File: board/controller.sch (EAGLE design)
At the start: 70 parts, among them J1 X, J10 FEED_HOLD, J11 PROBE, J12 ERROR, J13 HOLDING, J14 GND, J15 MOTOR_CURRENT, J16 SD_READER, J17 WHEEL, J18 FEED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

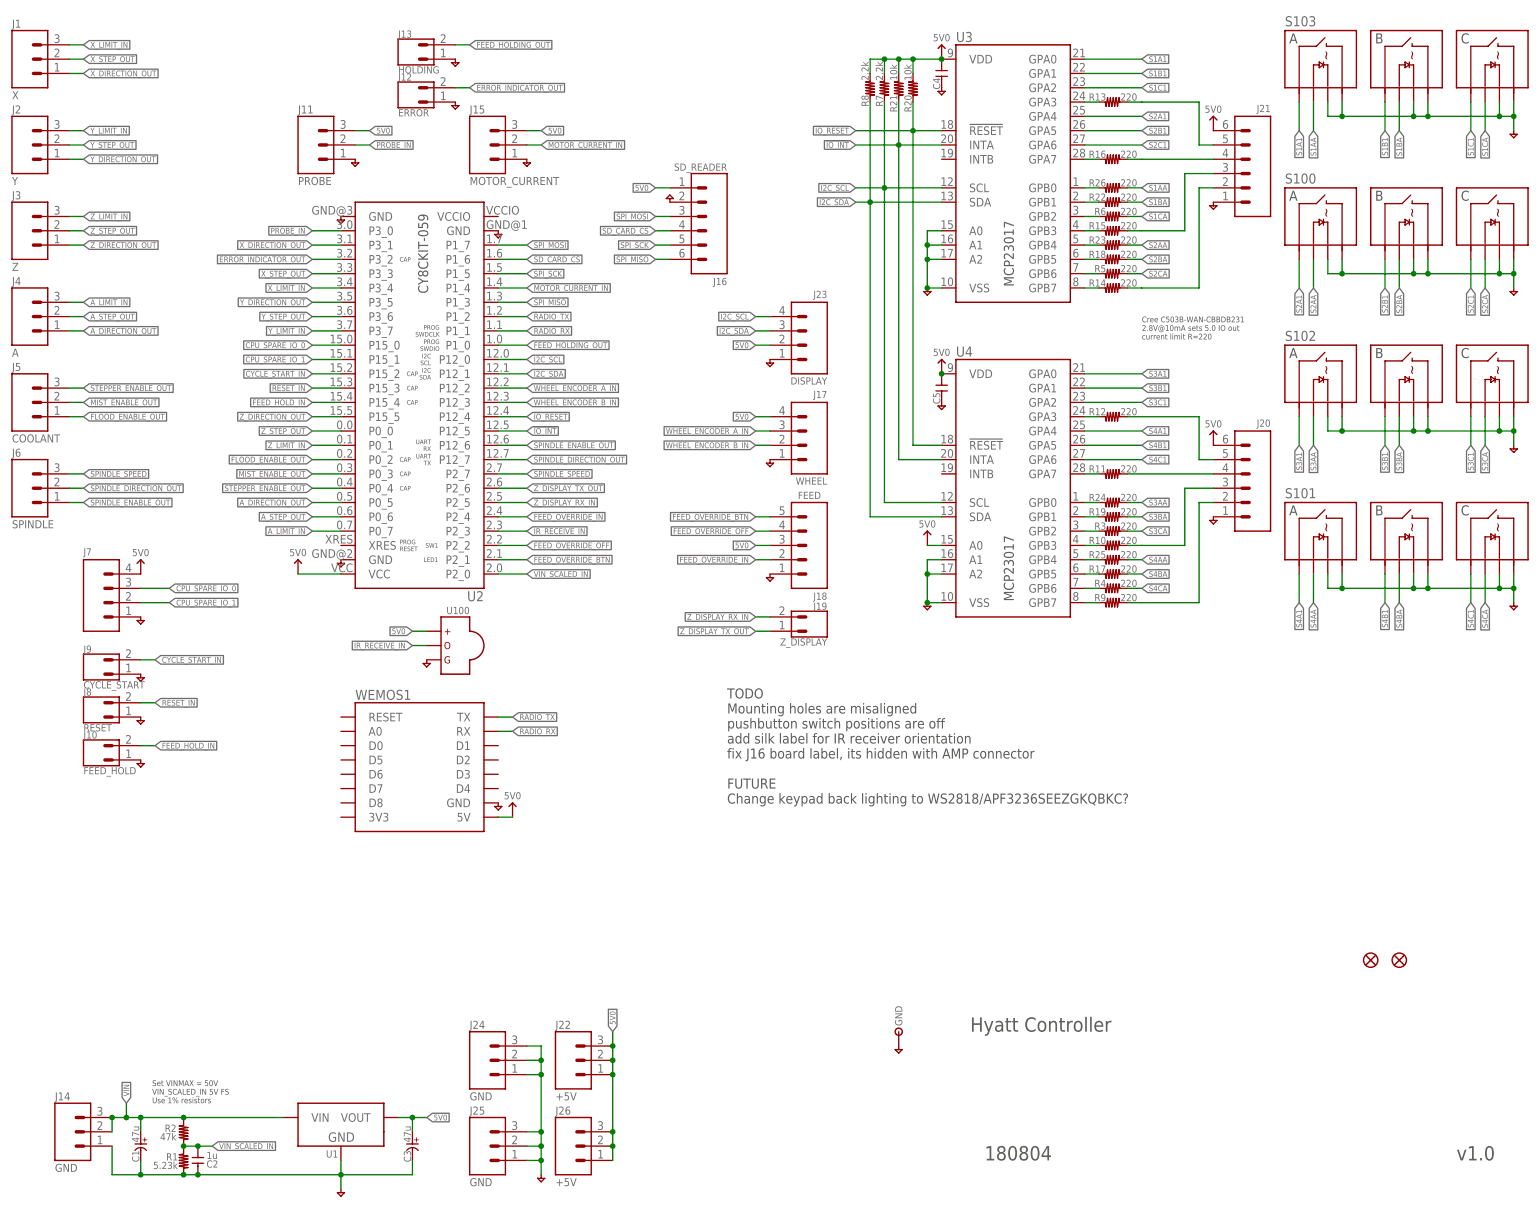
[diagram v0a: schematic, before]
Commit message: a little cleaning in main.c started v1.1 of schematic, v1.0 boards need blue-wired
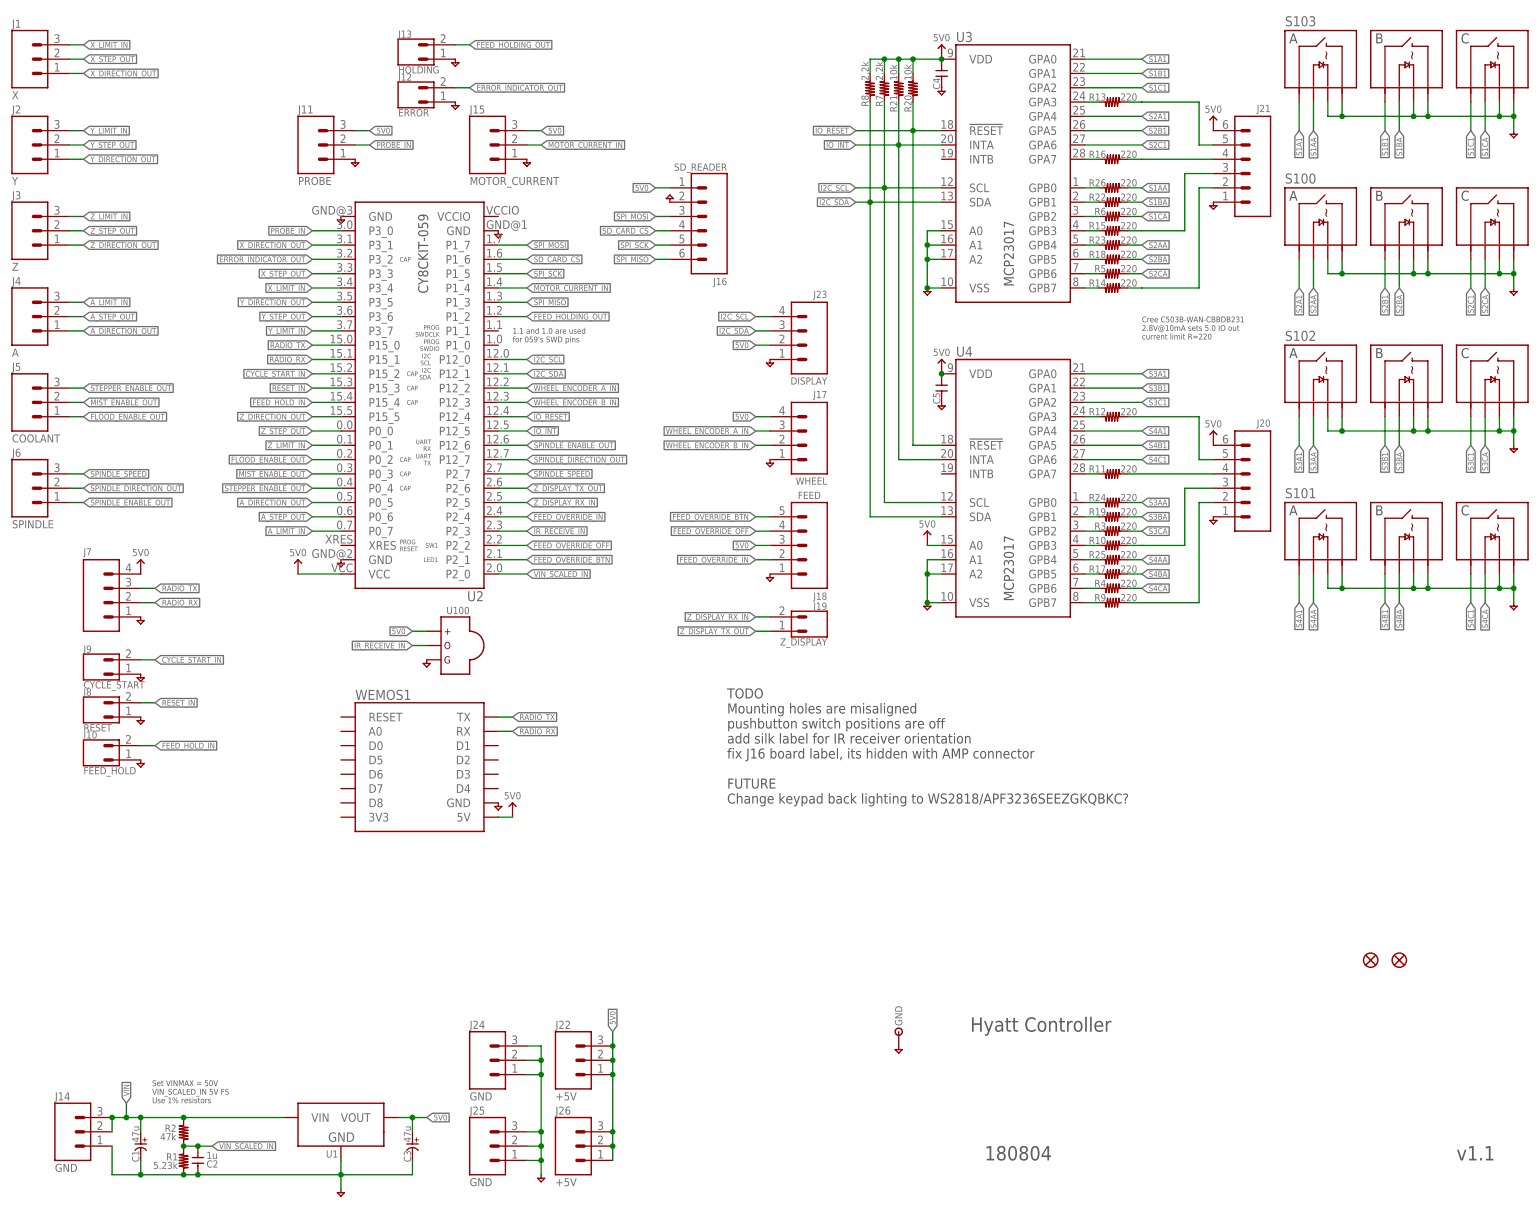
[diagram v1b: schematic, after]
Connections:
- removed net CPU_SPARE_IO_0: J7.3, U2.P15_0
- removed net CPU_SPARE_IO_1: J7.2, U2.P15_1
- net FEED_HOLDING_OUT: now also U2.P1_2; no longer U2.P1_0
- net RADIO_RX: now also J7.2, U2.P15_1; no longer U2.P1_1
- net RADIO_TX: now also J7.3, U2.P15_0; no longer U2.P1_2
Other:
- note added: "1.1 and 1.0 are used for 059's SWD pins"
- note added: "v1.1"
- note removed: "v1.0"
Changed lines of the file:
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@@
 <setting verticaltext="up"/>
 </settings>
-<grid distance="0.1" unitdist="inch" unit="inch" style="lines" multiple="1" display="yes" altdistance="0.01" altunitdist="inch" altunit="inch"/>
+<grid distance="0.1" unitdist="inch" unit="inch" style="lines" multiple="1" display="no" altdistance="0.01" altunitdist="inch" altunit="inch"/>
 <layers>
 <layer number="1" name="Top" color="4" fill="1" visible="no" active="no"/>
@@
 <text x="175.26" y="33.02" size="2.54" layer="97" align="top-left">Hyatt Controller</text>
 <text x="177.8" y="10.16" size="2.54" layer="97" align="top-left">180804</text>
-<text x="261.62" y="10.16" size="2.54" layer="97" align="top-left">v1.0</text>
+<text x="261.62" y="10.16" size="2.54" layer="97" align="top-left">v1.1</text>
 <text x="132.08" y="91.44" size="1.778" layer="97" align="top-left">TODO
 Mounting holes are misaligned
@@
 VIN_SCALED_IN 5V FS
 Use 1% resistors</text>
+<text x="93.98" y="155.448" size="1.016" layer="97" align="top-left">1.1 and 1.0 are used
+for 059's SWD pins</text>
 </plain>
 <instances>
@@
 </segment>
 <segment>
-<pinref part="U2" gate="G$1" pin="P1_0"/>
-<wire x1="91.44" y1="152.4" x2="96.52" y2="152.4" width="0.1524" layer="91"/>
-<label x="96.52" y="152.4" size="1.016" layer="95" xref="yes"/>
+<label x="96.52" y="157.48" size="1.016" layer="95" xref="yes"/>
+<pinref part="U2" gate="G$1" pin="P1_2"/>
+<wire x1="91.44" y1="157.48" x2="96.52" y2="157.48" width="0.1524" layer="91"/>
 </segment>
 </net>
@@
 </segment>
 <segment>
-<pinref part="U2" gate="G$1" pin="P1_2"/>
-<wire x1="91.44" y1="157.48" x2="96.52" y2="157.48" width="0.1524" layer="91"/>
-<label x="96.52" y="157.48" size="1.016" layer="95" xref="yes"/>
+<pinref part="U2" gate="G$1" pin="P15_0"/>
+<wire x1="63.5" y1="152.4" x2="58.42" y2="152.4" width="0.1524" layer="91"/>
+<label x="58.42" y="152.4" size="1.016" layer="95" rot="R180" xref="yes"/>
+</segment>
+<segment>
+<pinref part="J7" gate="G$1" pin="3"/>
+<wire x1="27.94" y1="109.22" x2="30.48" y2="109.22" width="0.1524" layer="91"/>
+<label x="30.48" y="109.22" size="1.016" layer="95" xref="yes"/>
 </segment>
 </net>
@@
 </segment>
 <segment>
-<pinref part="U2" gate="G$1" pin="P1_1"/>
-<wire x1="91.44" y1="154.94" x2="96.52" y2="154.94" width="0.1524" layer="91"/>
-<label x="96.52" y="154.94" size="1.016" layer="95" xref="yes"/>
+<pinref part="U2" gate="G$1" pin="P15_1"/>
+<wire x1="63.5" y1="149.86" x2="58.42" y2="149.86" width="0.1524" layer="91"/>
+<label x="58.42" y="149.86" size="1.016" layer="95" rot="R180" xref="yes"/>
+</segment>
+<segment>
+<pinref part="J7" gate="G$1" pin="2"/>
+<wire x1="27.94" y1="106.68" x2="30.48" y2="106.68" width="0.1524" layer="91"/>
+<label x="30.48" y="106.68" size="1.016" layer="95" xref="yes"/>
 </segment>
 </net>
@@
 </segment>
 </net>
-<net name="CPU_SPARE_IO_0" class="0">
-<segment>
-<pinref part="J7" gate="G$1" pin="3"/>
-<wire x1="27.94" y1="109.22" x2="33.02" y2="109.22" width="0.1524" layer="91"/>
-<label x="33.02" y="109.22" size="1.016" layer="95" xref="yes"/>
-</segment>
-<segment>
-<pinref part="U2" gate="G$1" pin="P15_0"/>
-<wire x1="63.5" y1="152.4" x2="58.42" y2="152.4" width="0.1524" layer="91"/>
-<label x="58.42" y="152.4" size="1.016" layer="95" rot="R180" xref="yes"/>
-</segment>
-</net>
-<net name="CPU_SPARE_IO_1" class="0">
-<segment>
-<pinref part="J7" gate="G$1" pin="2"/>
-<wire x1="27.94" y1="106.68" x2="33.02" y2="106.68" width="0.1524" layer="91"/>
-<label x="33.02" y="106.68" size="1.016" layer="95" xref="yes"/>
-</segment>
-<segment>
-<pinref part="U2" gate="G$1" pin="P15_1"/>
-<wire x1="58.42" y1="149.86" x2="63.5" y2="149.86" width="0.1524" layer="91"/>
-<label x="58.42" y="149.86" size="1.016" layer="95" rot="R180" xref="yes"/>
-</segment>
-</net>

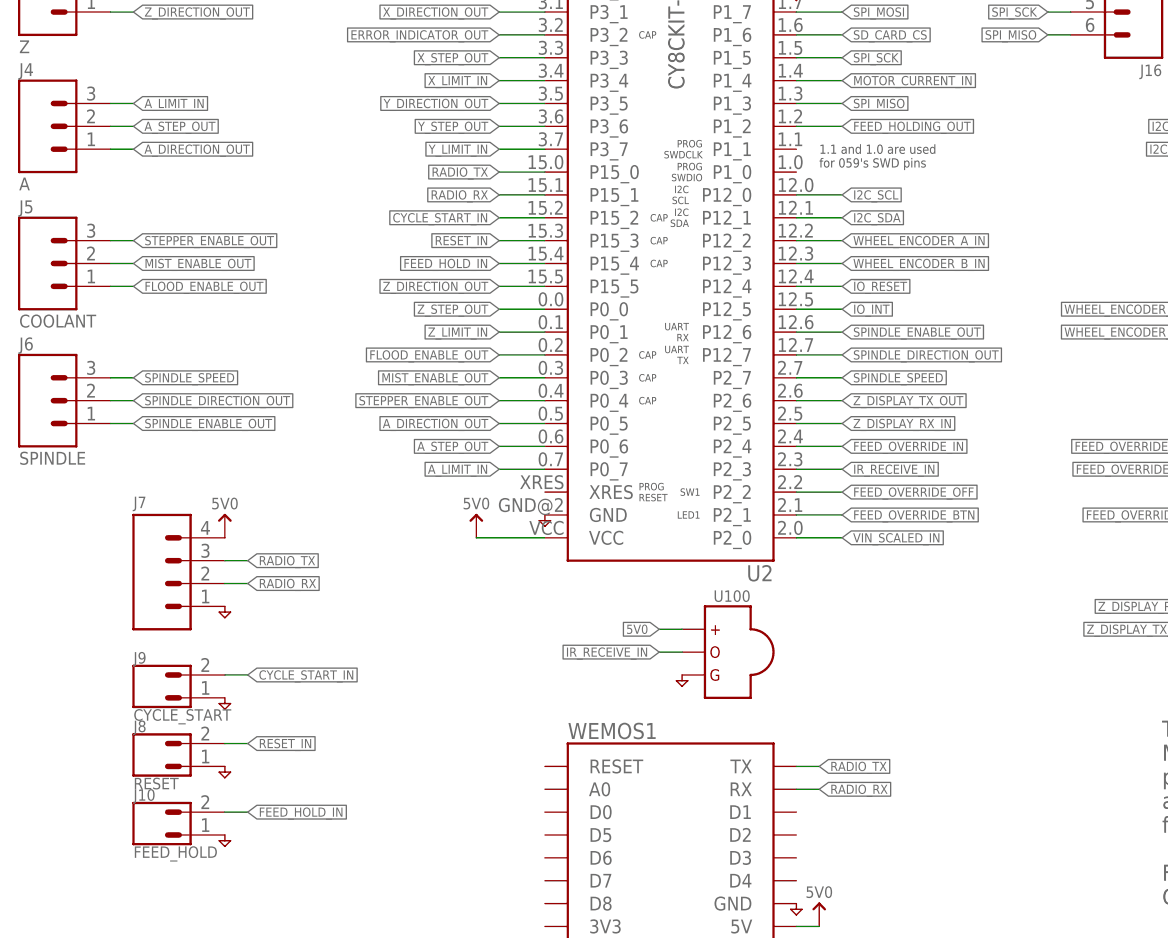
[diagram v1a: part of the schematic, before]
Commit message: updated several net names in schematic and psoc changed I2C to fixed instead of UDB
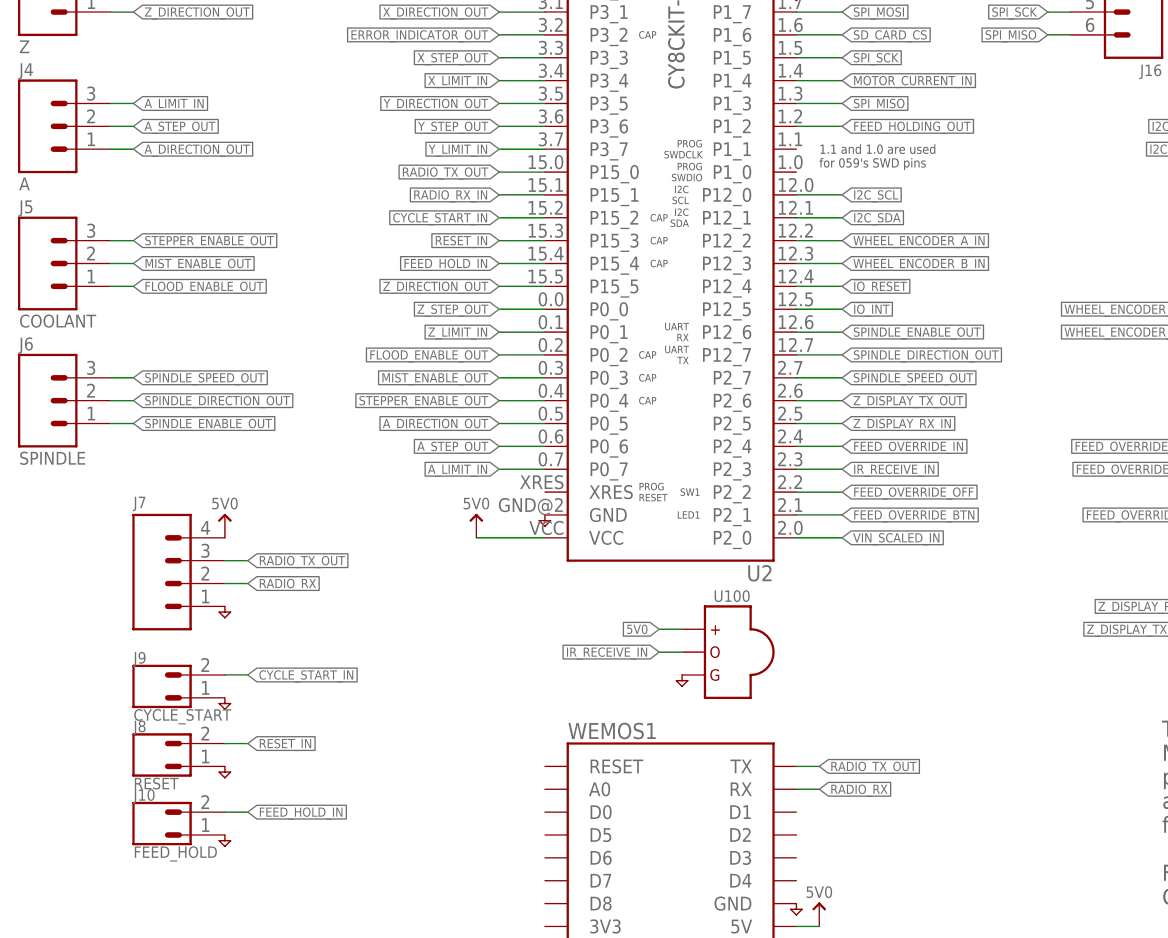
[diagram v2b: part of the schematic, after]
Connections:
- net RADIO_TX renamed RADIO_TX_OUT
- net SPINDLE_SPEED renamed SPINDLE_SPEED_OUT
- new net RADIO_RX_IN: U2.P15_1
- net RADIO_RX: no longer U2.P15_1
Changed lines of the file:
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@@
 </segment>
 </net>
-<net name="RADIO_TX" class="0">
+<net name="RADIO_TX_OUT" class="0">
 <segment>
 <pinref part="WEMOS1" gate="D1" pin="TX"/>
@@
 <wire x1="91.44" y1="83.82" x2="93.98" y2="83.82" width="0.1524" layer="91"/>
 <label x="93.98" y="83.82" size="1.016" layer="95" xref="yes"/>
-</segment>
-<segment>
-<pinref part="U2" gate="G$1" pin="P15_1"/>
-<wire x1="63.5" y1="149.86" x2="58.42" y2="149.86" width="0.1524" layer="91"/>
-<label x="58.42" y="149.86" size="1.016" layer="95" rot="R180" xref="yes"/>
 </segment>
 <segment>
@@
 </segment>
 </net>
-<net name="SPINDLE_SPEED" class="0">
+<net name="SPINDLE_SPEED_OUT" class="0">
 <segment>
 <wire x1="15.24" y1="129.54" x2="17.78" y2="129.54" width="0.1524" layer="91"/>
@@
 </segment>
 </net>
+<net name="RADIO_RX_IN" class="0">
+<segment>
+<pinref part="U2" gate="G$1" pin="P15_1"/>
+<wire x1="63.5" y1="149.86" x2="58.42" y2="149.86" width="0.1524" layer="91"/>
+<label x="58.42" y="149.86" size="1.016" layer="95" rot="R180" xref="yes"/>
+</segment>
+</net>

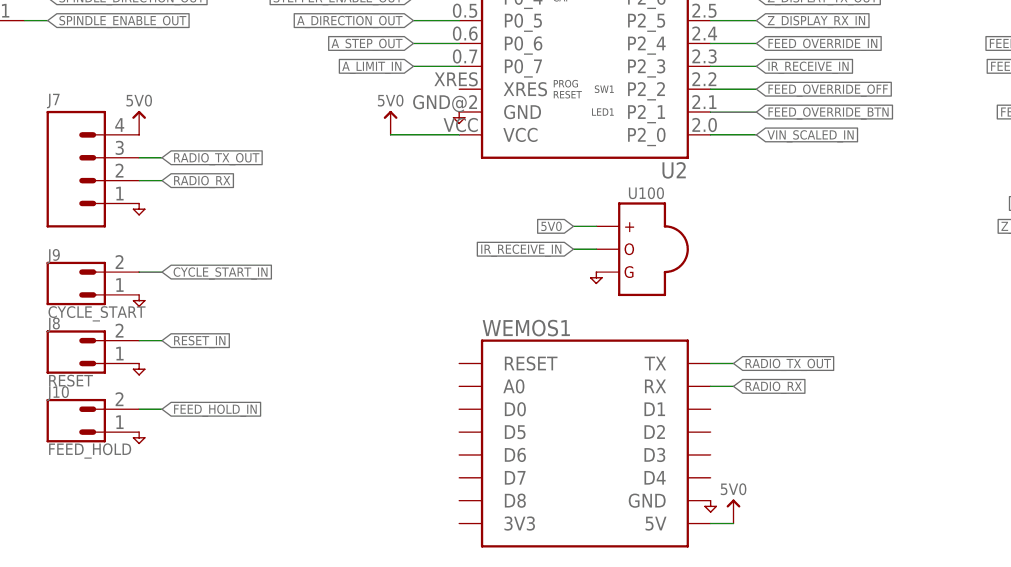
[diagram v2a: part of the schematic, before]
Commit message: updated a net name
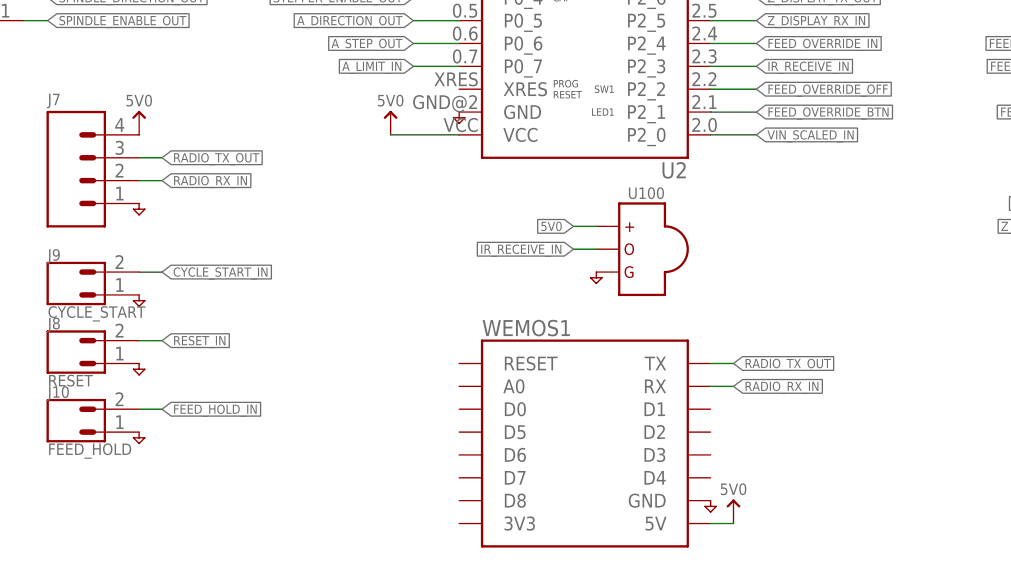
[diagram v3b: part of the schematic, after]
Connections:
- removed net RADIO_RX: J7.2, WEMOS1.RX
- net RADIO_RX_IN: now also J7.2, WEMOS1.RX
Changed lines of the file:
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@@
-</segment>
-</net>
-<net name="RADIO_RX" class="0">
-<segment>
-<pinref part="WEMOS1" gate="D1" pin="RX"/>
-<wire x1="91.44" y1="83.82" x2="93.98" y2="83.82" width="0.1524" layer="91"/>
-<label x="93.98" y="83.82" size="1.016" layer="95" xref="yes"/>
-</segment>
-<segment>
-<pinref part="J7" gate="G$1" pin="2"/>
-<wire x1="27.94" y1="106.68" x2="30.48" y2="106.68" width="0.1524" layer="91"/>
-<label x="30.48" y="106.68" size="1.016" layer="95" xref="yes"/>
 </segment>
 </net>
@@
 <label x="58.42" y="149.86" size="1.016" layer="95" rot="R180" xref="yes"/>
 </segment>
+<segment>
+<pinref part="WEMOS1" gate="D1" pin="RX"/>
+<wire x1="91.44" y1="83.82" x2="93.98" y2="83.82" width="0.1524" layer="91"/>
+<label x="93.98" y="83.82" size="1.016" layer="95" xref="yes"/>
+</segment>
+<segment>
+<pinref part="J7" gate="G$1" pin="2"/>
+<wire x1="27.94" y1="106.68" x2="30.48" y2="106.68" width="0.1524" layer="91"/>
+<label x="30.48" y="106.68" size="1.016" layer="95" xref="yes"/>
+</segment>
 </net>
